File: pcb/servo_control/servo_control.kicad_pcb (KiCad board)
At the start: 2 copper layers, 43 parts, among them J1 USB_B_Micro, J10 Conn_01x03_Female, J11 Conn_01x03_Female, J12 Conn_01x03_Female, J13 Conn_01x03_Female, J14 Conn_01x03_Female, J15 Conn_01x03_Female, J16 Conn_01x03_Female, J17 Conn_01x03_Female, J18 Conn_01x03_Female, J19 Conn_01x03_Female, J2 Conn_02x03_Counter_Clockwise, J20 Conn_01x03_Female, J21 Conn_01x06_Male, J3 Conn_01x03_Female, J4 Conn_01x03_Female, J5 Conn_01x03_Female, J6 Conn_01x03_Female, J7 Conn_01x03_Female, J8 Conn_01x03_Female, J9 Conn_01x03_Female, SW1 ESP_PROG, SW2 ESP_RST, U1 ATmega2560-16A, U2 LM317_SOT-223, U3 ESP32-WROOM-32, U4 MPU-9250

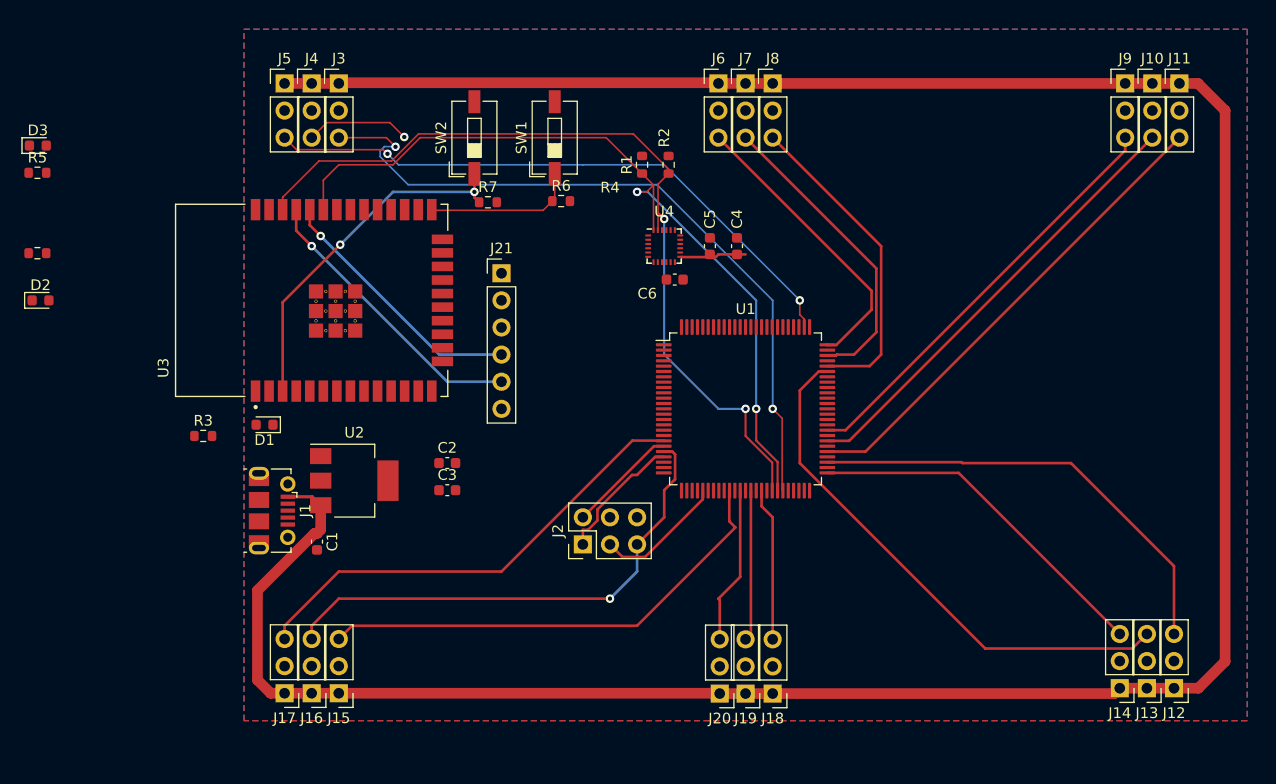
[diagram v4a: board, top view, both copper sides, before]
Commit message: wiring pcb for PCA9685
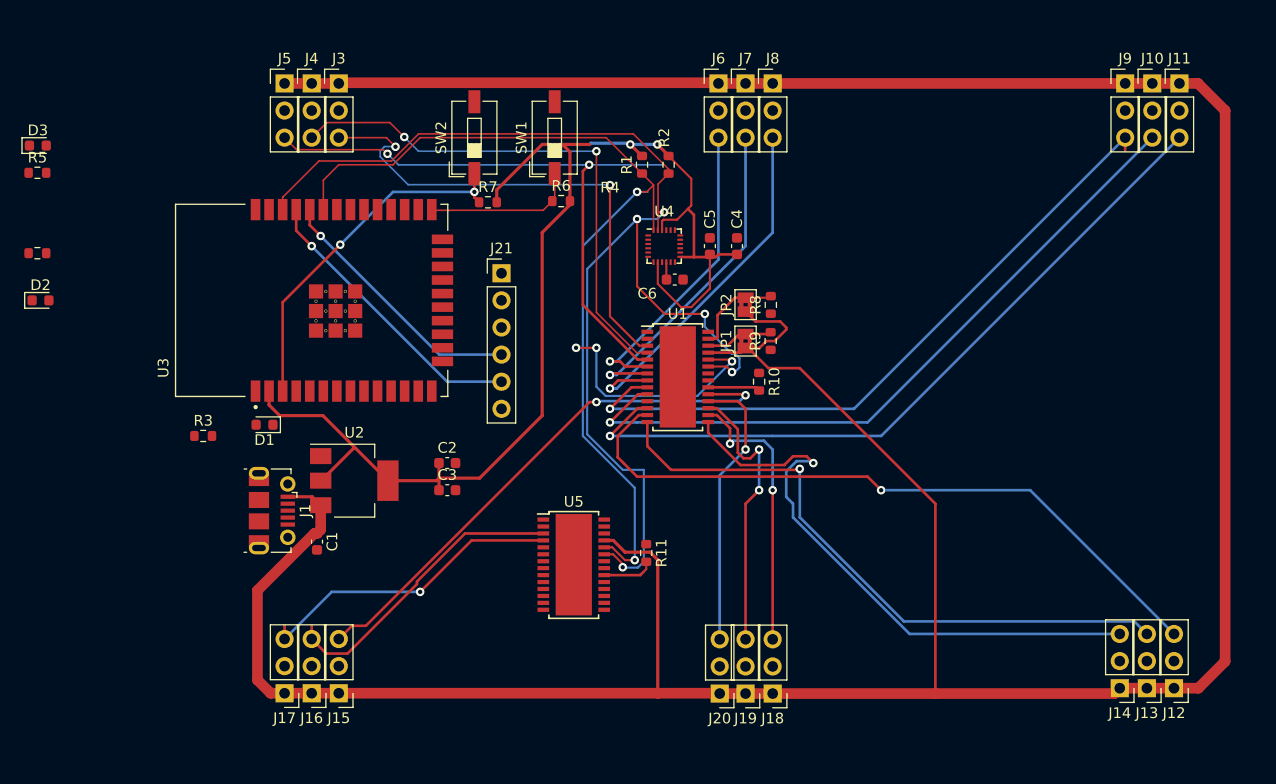
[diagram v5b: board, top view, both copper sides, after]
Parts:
- removed J2: Conn_02x03_Counter_Clockwise, Connector_PinHeader_2.54mm:PinHeader_2x03_P2.54mm_Vertical
- added JP1: Jumper_2_Open, Jumper:SolderJumper-2_P1.3mm_Bridged2Bar_Pad1.0x1.5mm, F.Cu at (147.3, 67.3)
- added JP2: Jumper_2_Open, Jumper:SolderJumper-2_P1.3mm_Bridged2Bar_Pad1.0x1.5mm, F.Cu at (147.3, 63.9)
- added R10: 10K, Resistor_SMD:R_0603_1608Metric, F.Cu at (148.6, 71.1)
- added R11: 10K, Resistor_SMD:R_0603_1608Metric, F.Cu at (138.0, 87.2)
- added R8: 10K, Resistor_SMD:R_0603_1608Metric, F.Cu at (149.7, 63.9)
- added R9: 10K, Resistor_SMD:R_0603_1608Metric, F.Cu at (149.7, 67.3)
- added U5: PCA9685BS, Package_SO:HTSSOP-28-1EP_4.4x9.7mm_P0.65mm_EP3.4x9.5mm, F.Cu at (131.2, 88.3)
- U1: value ATmega2560-16A -> PCA9685BS; footprint Package_QFP:TQFP-100_14x14mm_P0.5mm -> Package_SO:HTSSOP-28-1EP_4.4x9.7mm_P0.65mm_EP3.4x9.5mm
- moved U1 7.02 mm to (141.0, 70.7)
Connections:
- J10 pad 3: GPIO_33 -> PWM_0_7
- J11 pad 3: GPIO_35 -> PWM_0_8
- J12 pad 3: GPIO_37 -> PWM_0_9
- J13 pad 3: GPIO_39 -> PWM_0_10
- J14 pad 3: GPIO_41 -> PWM_0_11
- J15 pad 3: GPIO_49 -> PWM_0_15
- J16 pad 3: GPIO_51 -> PWM_1_0
- J17 pad 3: GPIO_53 -> PWM_1_1
- J18 pad 3: GPIO_43 -> PWM_0_12
- J19 pad 3: GPIO_45 -> PWM_0_13
- J20 pad 3: GPIO_47 -> PWM_0_14
- J3 pad 3: GPIO_19 -> PWM_0_0
- J4 pad 3: GPIO_21 -> PWM_0_1
- J5 pad 3: GPIO_23 -> PWM_0_2
- J6 pad 3: GPIO_25 -> PWM_0_3
- J7 pad 3: GPIO_27 -> PWM_0_4
- J8 pad 3: GPIO_29 -> PWM_0_5
- J9 pad 3: GPIO_31 -> PWM_0_6
- U1 pad 1: unconnected-(U1-Pad1) -> GND
- U1 pad 10: VCC -> PWM_0_7
- U1 pad 12: unconnected-(U1-Pad12) -> PWM_0_8
- U1 pad 13: unconnected-(U1-Pad13) -> PWM_0_9
- U1 pad 14: unconnected-(U1-Pad14) -> PWM_0_10
- U1 pad 15: unconnected-(U1-Pad15) -> PWM_0_11
- U1 pad 16: unconnected-(U1-Pad16) -> PWM_0_12
- U1 pad 17: unconnected-(U1-Pad17) -> PWM_0_13
- U1 pad 18: unconnected-(U1-Pad18) -> PWM_0_14
- U1 pad 19: GPIO_53 -> PWM_0_15
- U1 pad 2: unconnected-(U1-Pad2) -> GND
- U1 pad 20: GPIO_52 -> Net-(R10-Pad2)
- U1 pad 21: GPIO_51 -> GND
- U1 pad 22: GPIO_50 -> GND
- U1 pad 23: GPIO_10 -> I2C_SCL
- U1 pad 24: GPIO_11 -> I2C_SDA
- U1 pad 25: GPIO_12 -> VCC
- U1 pad 26: GPIO_13 -> FIRST_A0
- U1 pad 27: unconnected-(U1-Pad27) -> FIRST_A1
- U1 pad 28: unconnected-(U1-Pad28) -> GND
- U1 pad 29: unconnected-(U1-Pad29) -> GND
- U1 pad 3: unconnected-(U1-Pad3) -> PWM_0_0
- U1 pad 4: unconnected-(U1-Pad4) -> PWM_0_1
- U1 pad 5: unconnected-(U1-Pad5) -> PWM_0_2
- U1 pad 6: unconnected-(U1-Pad6) -> PWM_0_3
- U1 pad 7: unconnected-(U1-Pad7) -> PWM_0_4
- U1 pad 8: unconnected-(U1-Pad8) -> PWM_0_5
- U1 pad 9: unconnected-(U1-Pad9) -> PWM_0_6
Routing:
- net 3.3V: track 6.15 -> 118.8 mm, vias 0 -> 2
- net VCC: track 255.6 -> 329.3 mm
- net PWM_0_8: track 0.00 -> 69.5 mm, vias 0 -> 1
- net GPIO_19: track 68.4 -> 0.00 mm, vias 2 -> 0
- net PWM_0_7: track 0.00 -> 66.4 mm, vias 0 -> 1
- net PWM_0_9: track 0.00 -> 64.5 mm, vias 0 -> 1
- net PWM_0_6: track 0.00 -> 64.3 mm, vias 0 -> 1
- net PWM_0_10: track 0.00 -> 59.1 mm, vias 0 -> 1
- net PWM_0_2: track 0.00 -> 58.1 mm, vias 0 -> 2
- net GPIO_23: track 57.2 -> 0.00 mm, vias 2 -> 0
- net PWM_0_11: track 0.00 -> 55.4 mm, vias 0 -> 1
- net PWM_0_15: track 0.00 -> 51.1 mm, vias 0 -> 2
- net GPIO_39: track 50.4 -> 0.00 mm
- net PWM_0_1: track 0.00 -> 49.8 mm, vias 0 -> 2
- net GPIO_51: track 47.4 -> 0.00 mm, vias 1 -> 0
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- removed copper zone on B.Cu, net GND
- removed copper zone on F.Cu, net GND

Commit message: finish pcb
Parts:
- removed D3: LED, LED_SMD:LED_0603_1608Metric
- removed R5: 1K, Resistor_SMD:R_0603_1608Metric
- moved R4 35.5 mm to (112.2, 75.9)
- moved D2 25.7 mm to (102.7, 77.6)
- moved R3 14.1 mm to (110.5, 74.3), turned to 180 degrees
- moved R10 1.42 mm to (149.9, 71.8)
- moved C6 1.02 mm to (139.9, 62.2), turned to -90 degrees
- moved D1 0.79 mm to (102.7, 75.8), turned to 0 degrees
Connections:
- R3 pad 1: unconnected-(R3-Pad1) -> LED_1
- R4 pad 1: unconnected-(R4-Pad1) -> LED_2
- U3 pad 8: unconnected-(U3-Pad8) -> LED_2
- U3 pad 9: unconnected-(U3-Pad9) -> LED_1
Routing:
- net GND: track 0.00 -> 23.4 mm, vias 0 -> 28
- net Net-(D2-Pad2): track 0.00 -> 13.0 mm, vias 0 -> 2
- net Net-(D1-Pad2): track 0.00 -> 6.87 mm, vias 0 -> 2
- net PWM_0_11: track 55.4 -> 50.5 mm
- net LED_2: track 0.00 -> 4.34 mm
- net I2C_SCL: track 116.3 -> 119.9 mm
- net I2C_SDA: track 109.0 -> 111.8 mm
- net LED_1: track 0.00 -> 2.40 mm
- net Net-(R10-Pad2): track 4.89 -> 6.43 mm
- net PWM_0_7: track 66.4 -> 67.7 mm
- net PWM_0_8: track 69.5 -> 70.4 mm
- net PWM_0_10: track 59.1 -> 58.3 mm
- net 3.3V: track 118.8 -> 118.1 mm, vias 2 -> 5
- added copper zone on B.Cu, net GND
- added copper zone on F.Cu, net GND
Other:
- board outline added: 94.6 x 62.9 mm

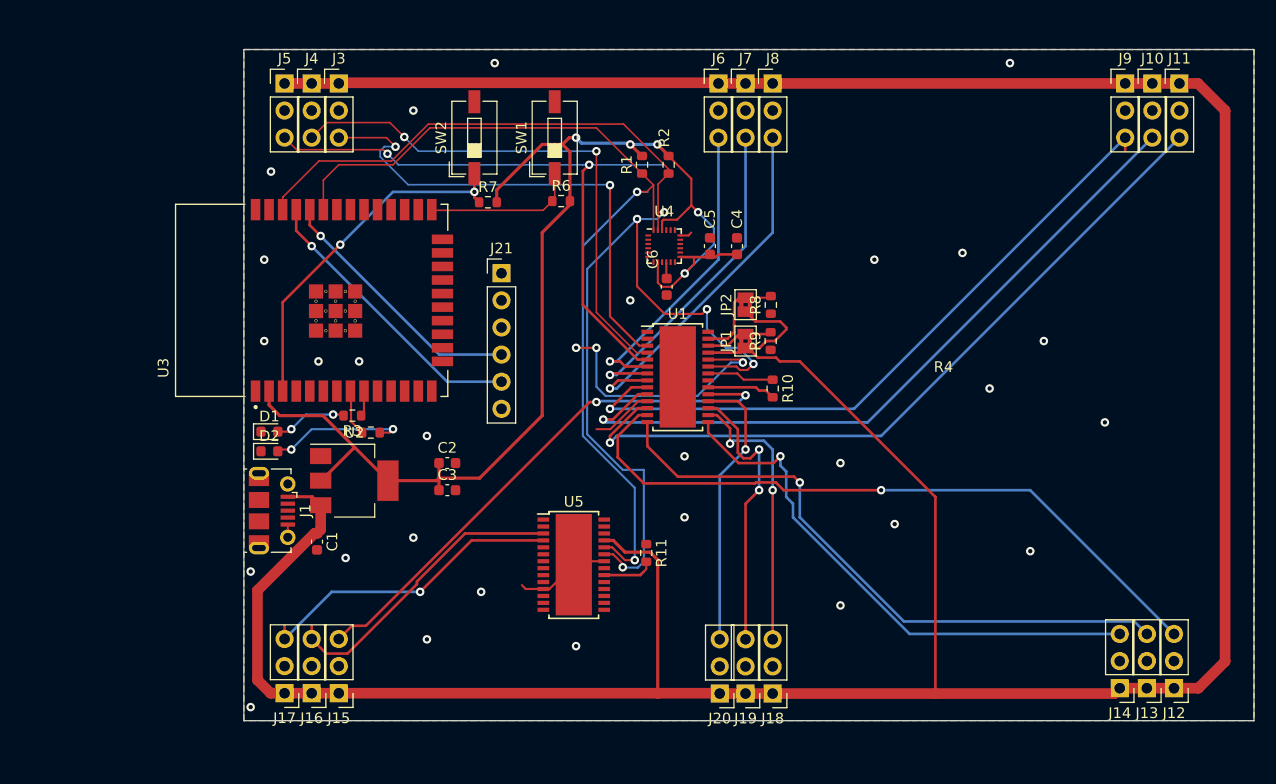
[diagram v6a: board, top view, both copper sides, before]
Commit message: fix servo header
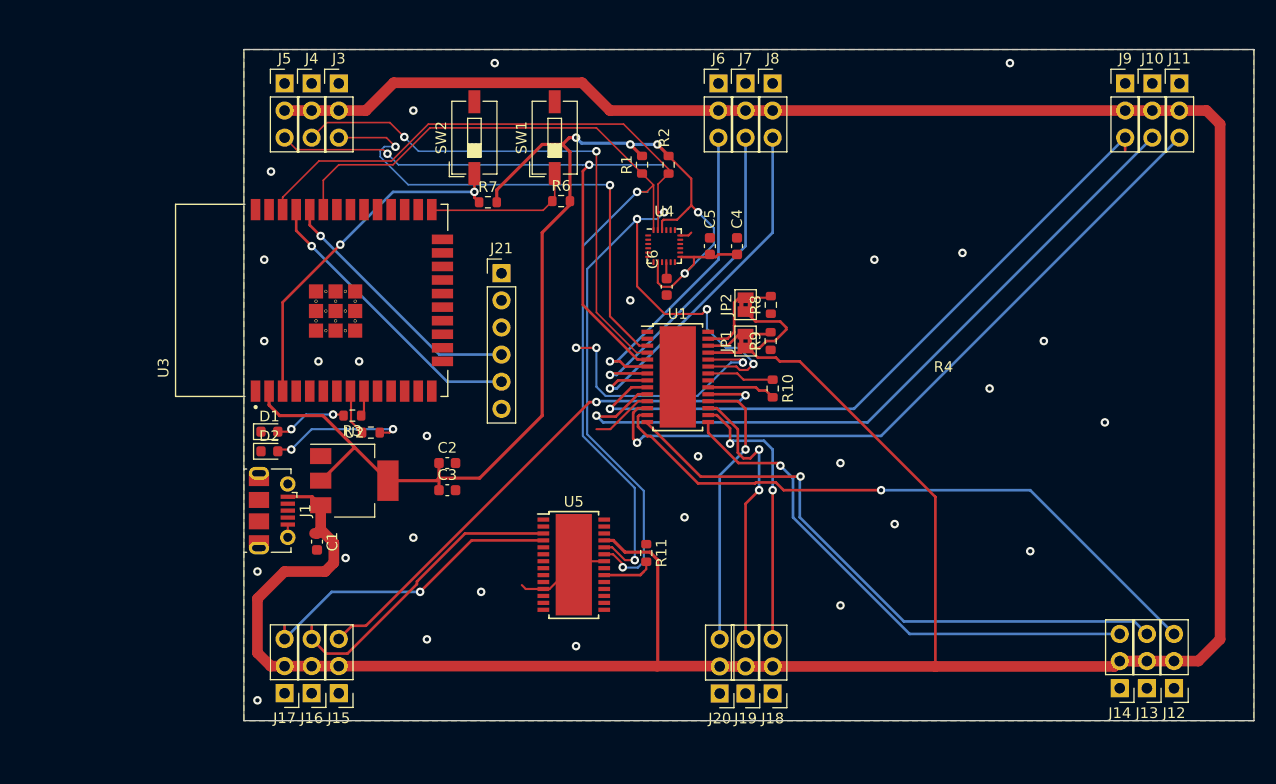
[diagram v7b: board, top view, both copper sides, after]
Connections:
- J10 pad 1: VCC -> GND
- J10 pad 2: GND -> VCC
- J11 pad 1: VCC -> GND
- J11 pad 2: GND -> VCC
- J12 pad 1: VCC -> GND
- J12 pad 2: GND -> VCC
- J13 pad 1: VCC -> GND
- J13 pad 2: GND -> VCC
- J14 pad 1: VCC -> GND
- J14 pad 2: GND -> VCC
- J15 pad 1: VCC -> GND
- J15 pad 2: GND -> VCC
- J16 pad 1: VCC -> GND
- J16 pad 2: GND -> VCC
- J17 pad 1: VCC -> GND
- J17 pad 2: GND -> VCC
- J18 pad 1: VCC -> GND
- J18 pad 2: GND -> VCC
- J19 pad 1: VCC -> GND
- J19 pad 2: GND -> VCC
- J20 pad 1: VCC -> GND
- J20 pad 2: GND -> VCC
- J3 pad 1: VCC -> GND
- J3 pad 2: GND -> VCC
- J4 pad 1: VCC -> GND
- J4 pad 2: GND -> VCC
- J5 pad 1: VCC -> GND
- J5 pad 2: GND -> VCC
- J6 pad 1: VCC -> GND
- J6 pad 2: GND -> VCC
- J7 pad 1: VCC -> GND
- J7 pad 2: GND -> VCC
- J8 pad 1: VCC -> GND
- J8 pad 2: GND -> VCC
- J9 pad 1: VCC -> GND
- J9 pad 2: GND -> VCC
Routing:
- net VCC: track 329.7 -> 324.3 mm
- net PWM_0_9: track 64.6 -> 60.2 mm
- net PWM_0_8: track 70.4 -> 67.1 mm
- net PWM_0_7: track 67.7 -> 69.1 mm
- net I2C_SCL: track 119.9 -> 118.7 mm
- net PWM_0_11: track 50.5 -> 49.5 mm
- net PWM_0_10: track 58.3 -> 57.4 mm

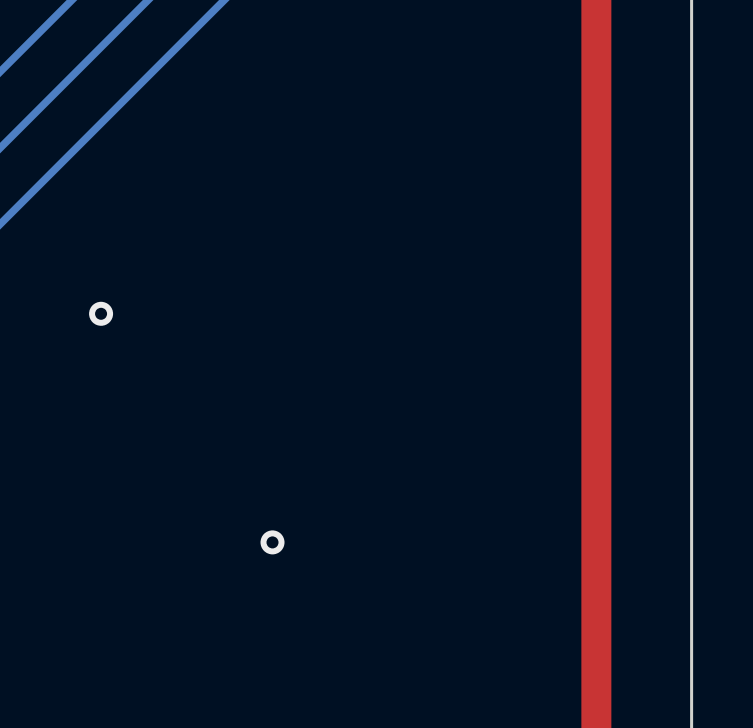
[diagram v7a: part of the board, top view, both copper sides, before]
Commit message: edit project name
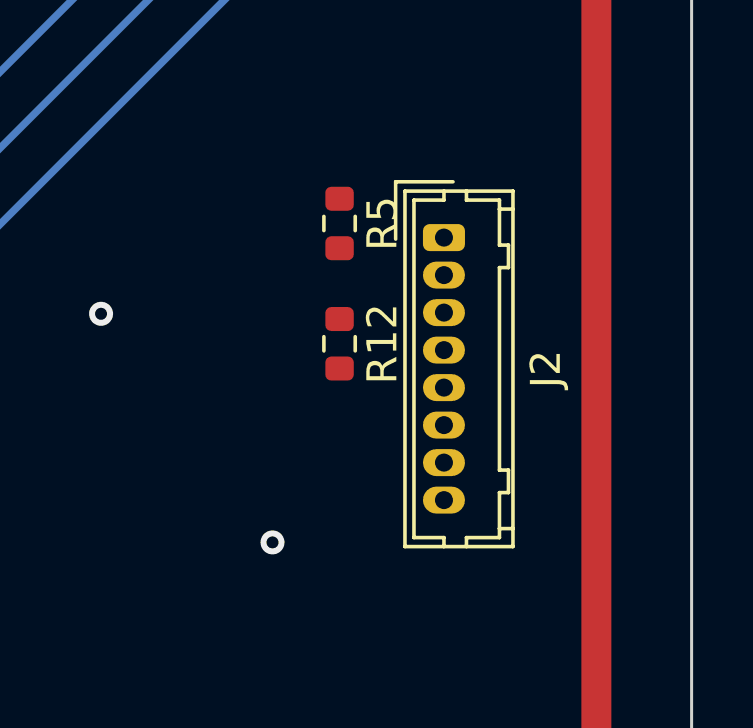
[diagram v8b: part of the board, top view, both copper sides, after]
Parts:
- added J2: YLIDAR X4, Connector_Hirose:Hirose_DF13-08P-1.25DSA_1x08_P1.25mm_Vertical, F.Cu at (186.7, 64.8)
- added R12: 10K, Resistor_SMD:R_0603_1608Metric, F.Cu at (183.2, 68.3)
- added R5: 10K, Resistor_SMD:R_0603_1608Metric, F.Cu at (183.2, 64.3)
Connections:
- U3 pad 10: unconnected-(U3-Pad10) -> DEV_EN
- U3 pad 27: unconnected-(U3-Pad27) -> ESP_RX
- U3 pad 28: unconnected-(U3-Pad28) -> ESP_TX
- U3 pad 37: unconnected-(U3-Pad37) -> M_SCTR
